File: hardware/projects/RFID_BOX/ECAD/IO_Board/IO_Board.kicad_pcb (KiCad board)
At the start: 2 copper layers, 100 x 100 mm, 16 parts, among them J1 J_WAGO_2604-1103, J2 J_WAGO_2604-1103, K1 T92S11D12-24, U3 IC_IRM-10-24, U4 AMS1117-3.3, U5 IC_RFB-0505S, U6 MCP39F511A-E/MQ, U7 VO615A-1, U8 VO615A-1

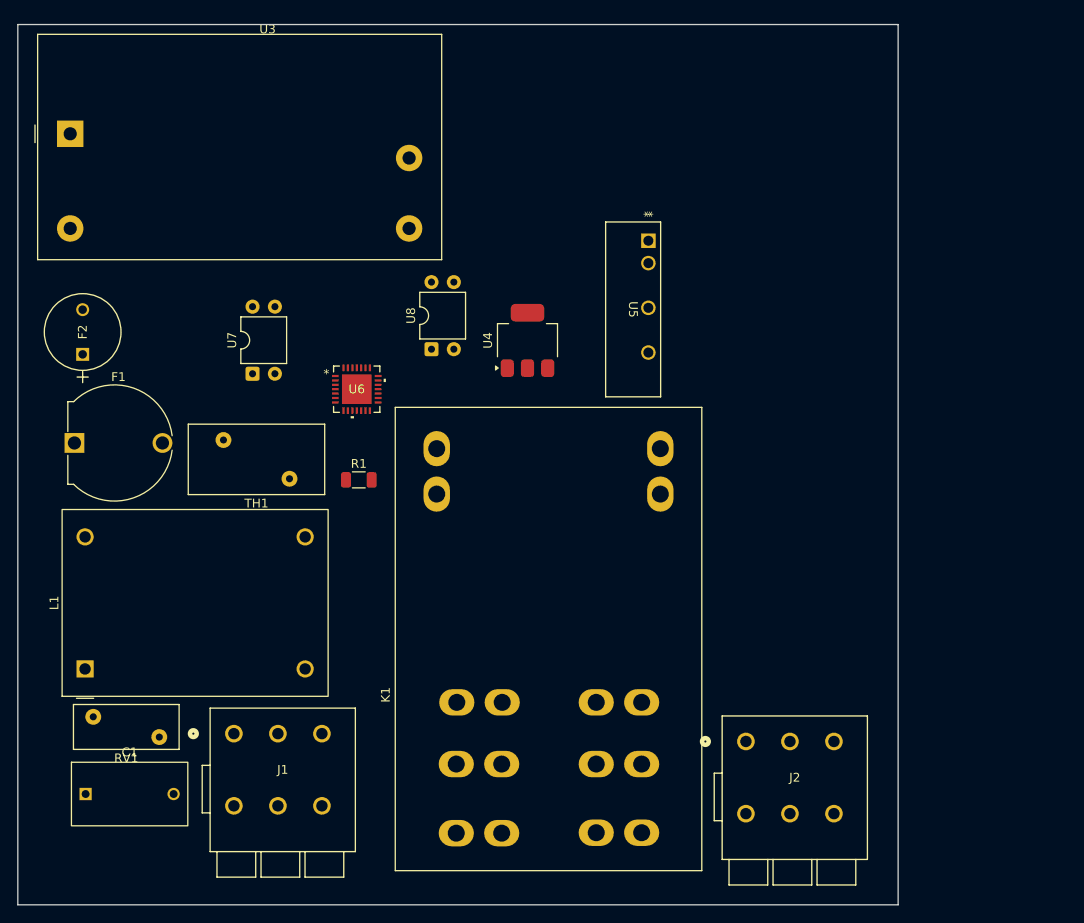
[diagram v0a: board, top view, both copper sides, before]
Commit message: Messinsel über isolierten Digitalisolator statt Kondensatornetzteil
Das Kondensatornetzteil der ISO-Messinsel entfällt. Der ISOW7721 (U300)
versorgt sie aus der SELV-Seite und führt zugleich die UART über die
Barriere; er ersetzt damit den LDO U302 und beide Optokoppler U304/U305.
Auslöser war der X2-Vorschaltkondensator, der im Flächenbudget des
I/O-Boards nicht unterzubringen war.

Die 8 mm Luft- und Kriechstrecke kommen jetzt aus dem Bauteil (VDE
0884-17, UL 1577 5 kVrms) statt aus einer Layoutforderung.

Schaltplan: U300 mit Abblockung C307–C317 und Ferriten FB300–FB307,
U302/U304/U305 entfernt.

README: Abschnitt 4 neu gefasst, Power-Distribution-Diagramm korrigiert
(Lastmessung liegt im N-Rückweg, nicht im gesicherten L-Pfad), BOM und
FMEA nachgezogen, U303 auf MCP39F511A-E/MQ berichtigt.

Ausserdem KiCad-Lock- und Autosave-Dateien in .gitignore aufgenommen.

Co-Authored-By: Claude Opus 5 <noreply@anthropic.com>
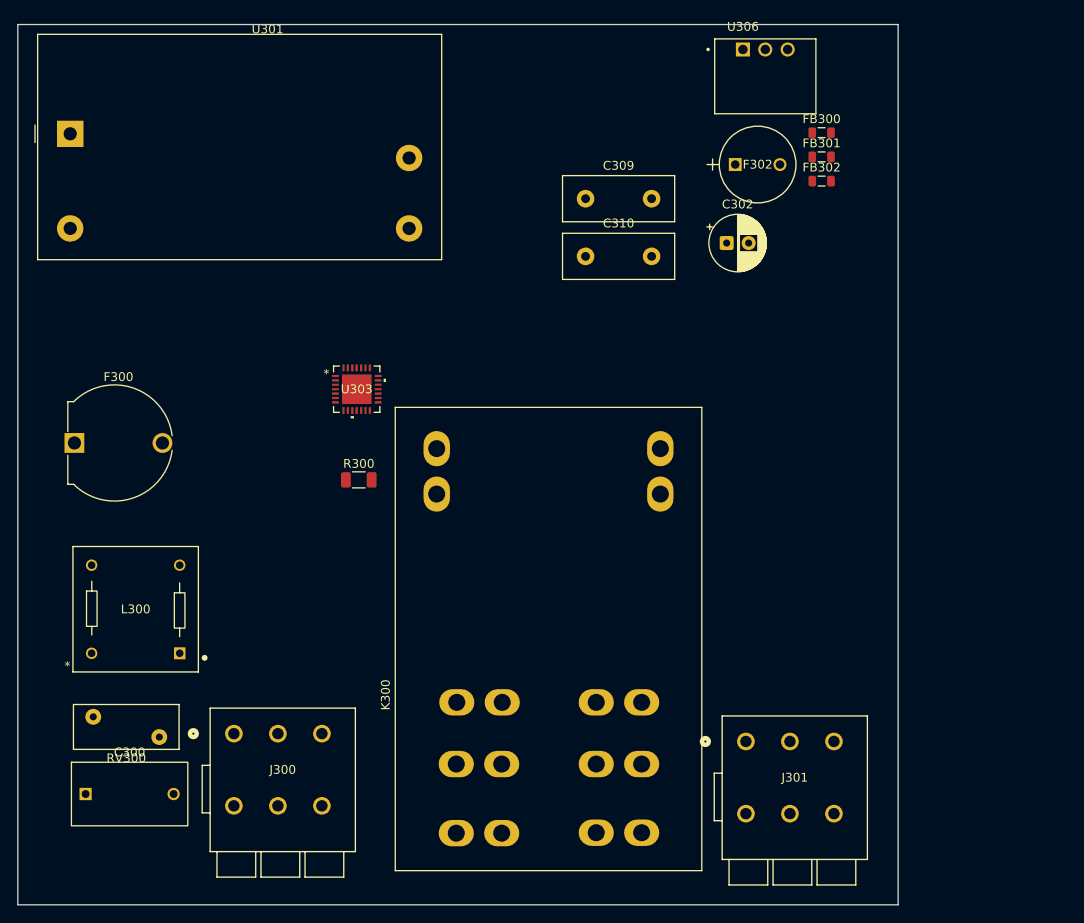
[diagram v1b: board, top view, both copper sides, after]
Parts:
- removed F2: 1A 250VAC, aa_MyParts:F_MRT_BEL
- removed L1: L_CMC_7448258022, aa_MyParts:L_Wurth_WE-CMB-XL
- removed TH1: ICL_BN-LG15Y2R5MYB, Varistor:RV_Disc_D15.5mm_W8mm_P7.5mm
- removed U4: AMS1117-3.3, Package_TO_SOT_SMD:SOT-223-3_TabPin2
- removed U5: IC_RFB-0505S, aa_MyParts:IC_RFB-0505S
- removed U7, U8: VO615A-1, Package_DIP:DIP-4_W7.62mm
- added C302: 47uF 50V, aa_MyParts:CP_Radial_D6.3mm_H11.0mm_P2.50mm, F.Cu at (156.7, 67.4)
- added C309: VY2472M49Y5US63L7, Capacitor_THT:C_Disc_D12.5mm_W5.0mm_P7.50mm, F.Cu at (140.7, 62.3)
- added C310: VY2472M49Y5US63L7, Capacitor_THT:C_Disc_D12.5mm_W5.0mm_P7.50mm, F.Cu at (140.7, 68.9)
- added F302: 500mA 250VAC, aa_MyParts:F_MRT_BEL, F.Cu at (157.7, 58.4)
- added FB300: 600R@100MHz, Inductor_SMD:L_0805_2012Metric, F.Cu at (167.5, 54.8)
- added FB301: 600R@100MHz, Inductor_SMD:L_0805_2012Metric, F.Cu at (167.5, 57.6)
- added FB302: 600R@100MHz, Inductor_SMD:L_0805_2012Metric, F.Cu at (167.5, 60.3)
- added L300: RN102-1-02-3M0, aa_MyParts:L_RN102_SCN, F.Cu at (84.6, 114.0)
- added U306: R-78K5.0-2.0, aa_MyParts:IC_CONV_R-78K5.0-2.0, F.Cu at (161.1, 48.4)
- R300: renamed from R1; value 20mR -> 2mR PA1206FRM670R002L
- U301: renamed from U3; value IC_IRM-10-24 -> IRM-10-24
- renumbered C1 to C300, F1 to F300, J1 to J300, J2 to J301, K1 to K300, RV1 to RV300, U6 to U303
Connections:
- F300 pad 1: /PIN_CMC_L -> /PIN_L
- J301 pad 3: Net-(J2-Pin_3) -> Net-(J301-Pin_3)
- J301 pad 4: Net-(J2-Pin_3) -> Net-(J301-Pin_3)
- K300 pad 0: unconnected-(K1-Pad0) -> (no net)
- K300 pad 1: unconnected-(K1-Pad1) -> (no net)
- K300 pad 4: Net-(U6-I1-) -> /PIN_FUSED_L
- K300 pad 6: unconnected-(K1-Pad6) -> Net-(J301-Pin_3)
- K300 pad 8: /PIN_CMC_N -> Net-(FB302-Pad2)
- R300 pad 1: Net-(U6-V1+) -> /PIN_N
- R300 pad 2: Net-(U6-I1-) -> Net-(FB302-Pad2)
- U301 pad 1: /PIN_CMC_N -> /PIN_CTRL_N
- U301 pad 2: Net-(U3-AC/L) -> /PIN_CTRL_L
- U301 pad 3: Net-(U3--Vo) -> GND
- U301 pad 4: unconnected-(U3-+Vo-Pad4) -> +24V
- U303 pad 12: Net-(U6-UART_TX) -> unconnected-(U303-UART_TX-Pad12)
- U303 pad 17: Net-(U6-I1-) -> Net-(U303-I1-)
- U303 pad 19: Net-(U6-V1+) -> Net-(U303-V1+)
- U303 pad 25: Net-(U4-VO) -> unconnected-(U303-DVDD-Pad25)
- U303 pad 29: Net-(U4-GND) -> GND_ISO
- U303 pad 4: Net-(U6-UART_RX) -> unconnected-(U303-UART_RX-Pad4)

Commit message: Relaistreiber bestueckt, README gestrafft
Treiber des Lastrelais vollstaendig ausgelegt: Low-Side-NMOS Q300 und
High-Side-PMOS Q301 in Reihe in der Spule, dazu Q302 als Pegelwandler
fuer den symmetrischen 47k/47k-Gate-Teiler von Q301. Die Symmetrie ist
zwingend, unsymmetrisch laege Vgs ueber dem Gate-Limit von +/-20V.

Bauteile: 2N7002NXAKR (Q300, Q302), BSS84AK (Q301), BAS16LT1G (D305).
D305 bleibt im SOT-23 statt SOD-323 — verdrehsicher und in der
Groessenklasse der 0603-Passiven. BOM-Summe 90,11 -> 90,00 EUR.

README: Kapitel "Versorgung und Isolation der Messinsel" und der
Relaistreiber-Abschnitt entfallen; die 4mm-Kupfersperrzone um VISOOUT
und die Ferrit-Trennung GND_ISO2/GND_ISO sind nach "Domaenen und
Abstaende" gewandert. Acht erledigte oder nicht mehr relevante
TODO-Eintraege geloescht.

Datenblaetter fuer die neuen Bauteile ergaenzt.

Co-Authored-By: Claude Opus 5 <noreply@anthropic.com>
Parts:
- removed U303: MCP39F511A-E/MQ, aa_MyParts:IC_QFN28_MQ_MCH
- added C301: 100nF 50V, Capacitor_SMD:C_0603_1608Metric, F.Cu at (159.1, 79.9)
- added C303: 10uF 10V 0805, Capacitor_SMD:C_0805_2012Metric, F.Cu at (166.8, 100.3)
- added C304: 10nF, Capacitor_SMD:C_0603_1608Metric, F.Cu at (159.1, 82.4)
- added C305: 1uF, Capacitor_SMD:C_0603_1608Metric, F.Cu at (159.1, 84.9)
- added C306: 10uF, Capacitor_SMD:C_0603_1608Metric, F.Cu at (159.1, 87.5)
- added C307: 10nF, Capacitor_SMD:C_0603_1608Metric, F.Cu at (159.1, 90.0)
- added C308: 1uF, Capacitor_SMD:C_0603_1608Metric, F.Cu at (159.1, 92.5)
- added C311: 10uF, Capacitor_SMD:C_0603_1608Metric, F.Cu at (159.1, 95.0)
- added C312: 10nF, Capacitor_SMD:C_0603_1608Metric, F.Cu at (159.1, 97.5)
- added C313: 1uF, Capacitor_SMD:C_0603_1608Metric, F.Cu at (163.1, 79.9)
- added C314: 10uF, Capacitor_SMD:C_0603_1608Metric, F.Cu at (163.1, 82.4)
- added C315: 10uF, Capacitor_SMD:C_0603_1608Metric, F.Cu at (163.1, 84.9)
- added C316: 1uF, Capacitor_SMD:C_0603_1608Metric, F.Cu at (163.1, 87.5)
- added C317: 10nF, Capacitor_SMD:C_0603_1608Metric, F.Cu at (163.1, 90.0)
- added C318: 33nF 50V, Capacitor_SMD:C_0603_1608Metric, F.Cu at (163.1, 92.5)
- added C319: 33nF 50V, Capacitor_SMD:C_0603_1608Metric, F.Cu at (163.1, 95.0)
- added C320: 33nF 50V, Capacitor_SMD:C_0603_1608Metric, F.Cu at (163.1, 97.5)
- added C321: 33nF 50V, Capacitor_SMD:C_0603_1608Metric, F.Cu at (167.1, 79.9)
- added C322: 1uF 10V, Capacitor_SMD:C_0603_1608Metric, F.Cu at (167.1, 82.4)
- added C323: 100nF 25V, Capacitor_SMD:C_0603_1608Metric, F.Cu at (167.1, 84.9)
- added C324: 100nF 25V, Capacitor_SMD:C_0603_1608Metric, F.Cu at (167.1, 87.5)
- added C325: 10uF, Capacitor_SMD:C_0603_1608Metric, F.Cu at (184.2, 59.7)
- added C326: 10uF 10V, Capacitor_SMD:C_0805_2012Metric, F.Cu at (166.8, 103.3)
- added C327: 100nF 25V, Capacitor_SMD:C_0603_1608Metric, F.Cu at (167.1, 90.0)
- added C328: 10uF 10V 0805, Capacitor_SMD:C_0805_2012Metric, F.Cu at (188.4, 68.3)
- added D300: D_BAS16LT1G, Package_TO_SOT_SMD:SOT-23, F.Cu at (179.8, 60.7)
- added FB303: 330R@100MHz, Inductor_SMD:L_0805_2012Metric, F.Cu at (175.4, 94.5)
- added FB304: 330R@100MHz, Inductor_SMD:L_0805_2012Metric, F.Cu at (175.4, 97.3)
- added FB305: 330R@100MHz, Inductor_SMD:L_0805_2012Metric, F.Cu at (175.4, 100.0)
- added FB306: 330R@100MHz, Inductor_SMD:L_0805_2012Metric, F.Cu at (175.4, 102.8)
- added FB307: 330R@100MHz, Inductor_SMD:L_0805_2012Metric, F.Cu at (175.4, 105.5)
- added NT300: NetTie, NetTie:NetTie-2_SMD_Pad0.5mm, F.Cu at (151.4, 83.5)
- added PS300: AP2114H-3.3TRG1, Package_TO_SOT_SMD:SOT-223-3_TabPin2, F.Cu at (191.1, 62.7)
- added Q300: 2N7002NXAKR, Package_TO_SOT_SMD:SOT-23, F.Cu at (179.8, 65.2)
- added Q301: BSS84AK, Package_TO_SOT_SMD:SOT-23, F.Cu at (179.8, 69.6)
- added Q302: 2N7002NXAKR, Package_TO_SOT_SMD:SOT-23, F.Cu at (179.8, 74.1)
- added R301: 1k, Resistor_SMD:R_0603_1608Metric, F.Cu at (167.1, 92.5)
- added R302: 1k, Resistor_SMD:R_0603_1608Metric, F.Cu at (167.1, 95.0)
- added R303: 499k, Resistor_SMD:R_2010_5025Metric, F.Cu at (181.4, 95.3)
- added R304: 499k, Resistor_SMD:R_2010_5025Metric, F.Cu at (181.4, 99.5)
- added R306: 1k, Resistor_SMD:R_0603_1608Metric, F.Cu at (167.1, 97.5)
- added R307: 10R, Resistor_SMD:R_0603_1608Metric, F.Cu at (171.1, 79.9)
- added R308: 2k, Resistor_SMD:R_0603_1608Metric, F.Cu at (171.1, 82.4)
- added R309: 2k, Resistor_SMD:R_0603_1608Metric, F.Cu at (171.1, 84.9)
- added R310: 2R49, Resistor_SMD:R_0603_1608Metric, F.Cu at (171.1, 87.5)
- added R311: 2k, Resistor_SMD:R_0603_1608Metric, F.Cu at (171.1, 90.0)
- added R312: 1k, Resistor_SMD:R_0603_1608Metric, F.Cu at (184.2, 62.2)
- added R313: 47k, Resistor_SMD:R_0603_1608Metric, F.Cu at (184.2, 64.8)
- added R314: 47k, Resistor_SMD:R_0603_1608Metric, F.Cu at (184.2, 67.3)
- added R315: 1k, Resistor_SMD:R_0603_1608Metric, F.Cu at (184.2, 69.8)
- added R316: 47k, Resistor_SMD:R_0603_1608Metric, F.Cu at (184.2, 72.3)
- added R317: 47k, Resistor_SMD:R_0603_1608Metric, F.Cu at (184.2, 74.8)
- added U300: ISOW7721DFMR, Package_SO:SOIC-20W_7.5x12.8mm_P1.27mm, F.Cu at (179.6, 86.0)
- added U302: MCP39F511A-E/MQ, aa_MyParts:IC_QFN28_MQ_MCH, F.Cu at (160.7, 102.4)
- R300: value 2mR PA1206FRM670R002L -> 2mR CRF2010-FZ-R002ELF; footprint Resistor_SMD:R_1206_3216Metric -> Resistor_SMD:R_2010_5025Metric
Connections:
- FB300 pad 1: unconnected-(FB300-Pad1) -> Net-(FB300-Pad1)
- K300 pad 0: (no net) -> Net-(D300-A)
- K300 pad 1: (no net) -> Net-(D300-K)
